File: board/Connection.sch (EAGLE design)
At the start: 42 parts, among them U1 NUCLEO-G431KB, U2 SN65HVD230, U5 ADA4528-1ARMZ-R7

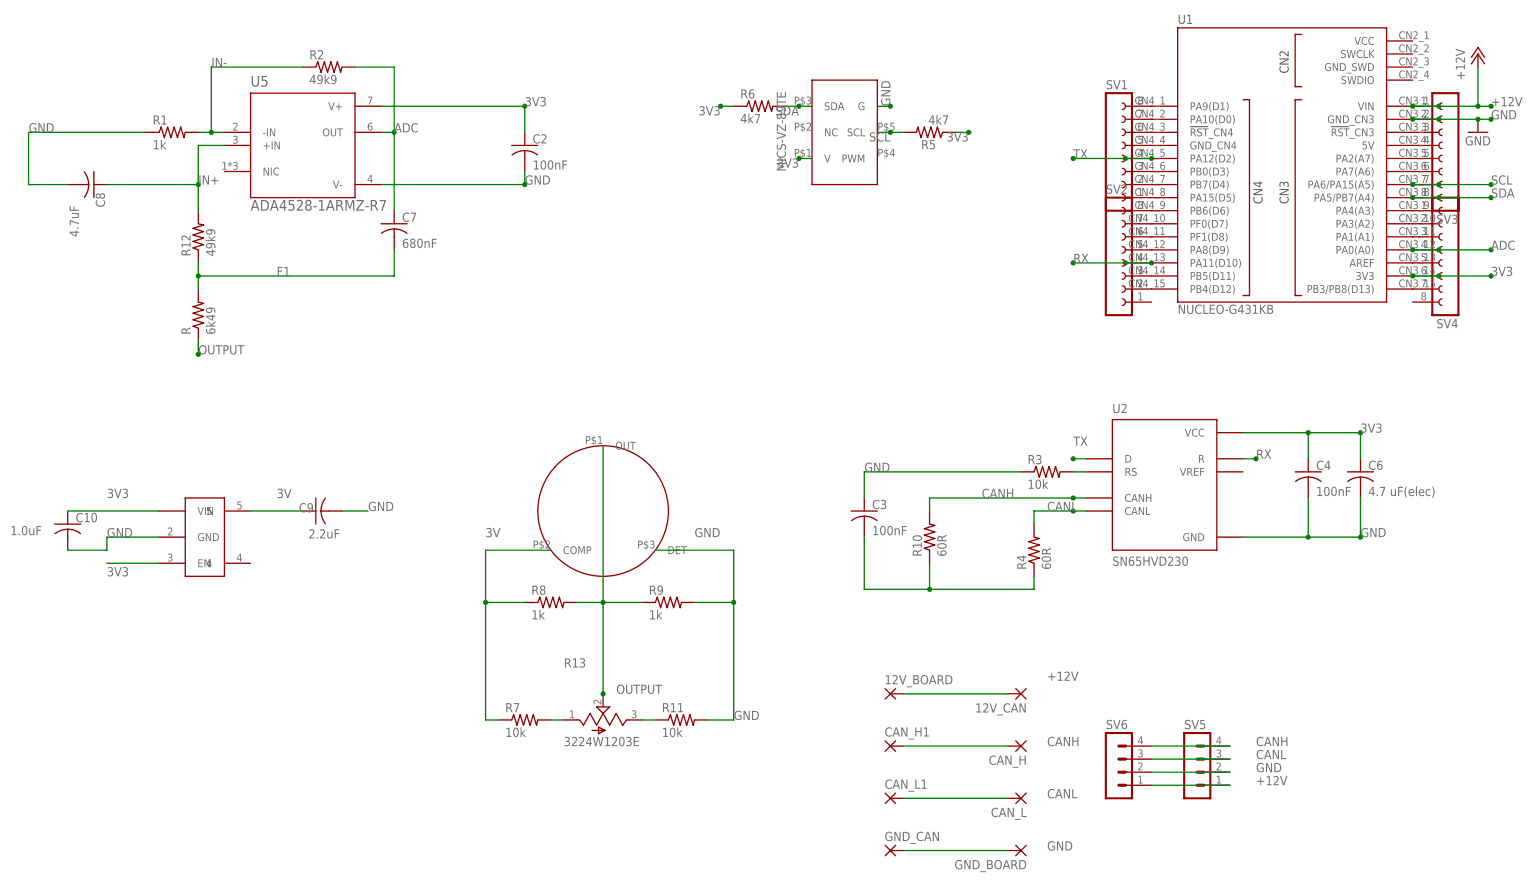
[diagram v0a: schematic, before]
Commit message: move ch4 sensor away from nucleo female header pins for nucleo insertion move the 4pin CAN away from top of the nucleo space the other CAN pins to fit a terminal block
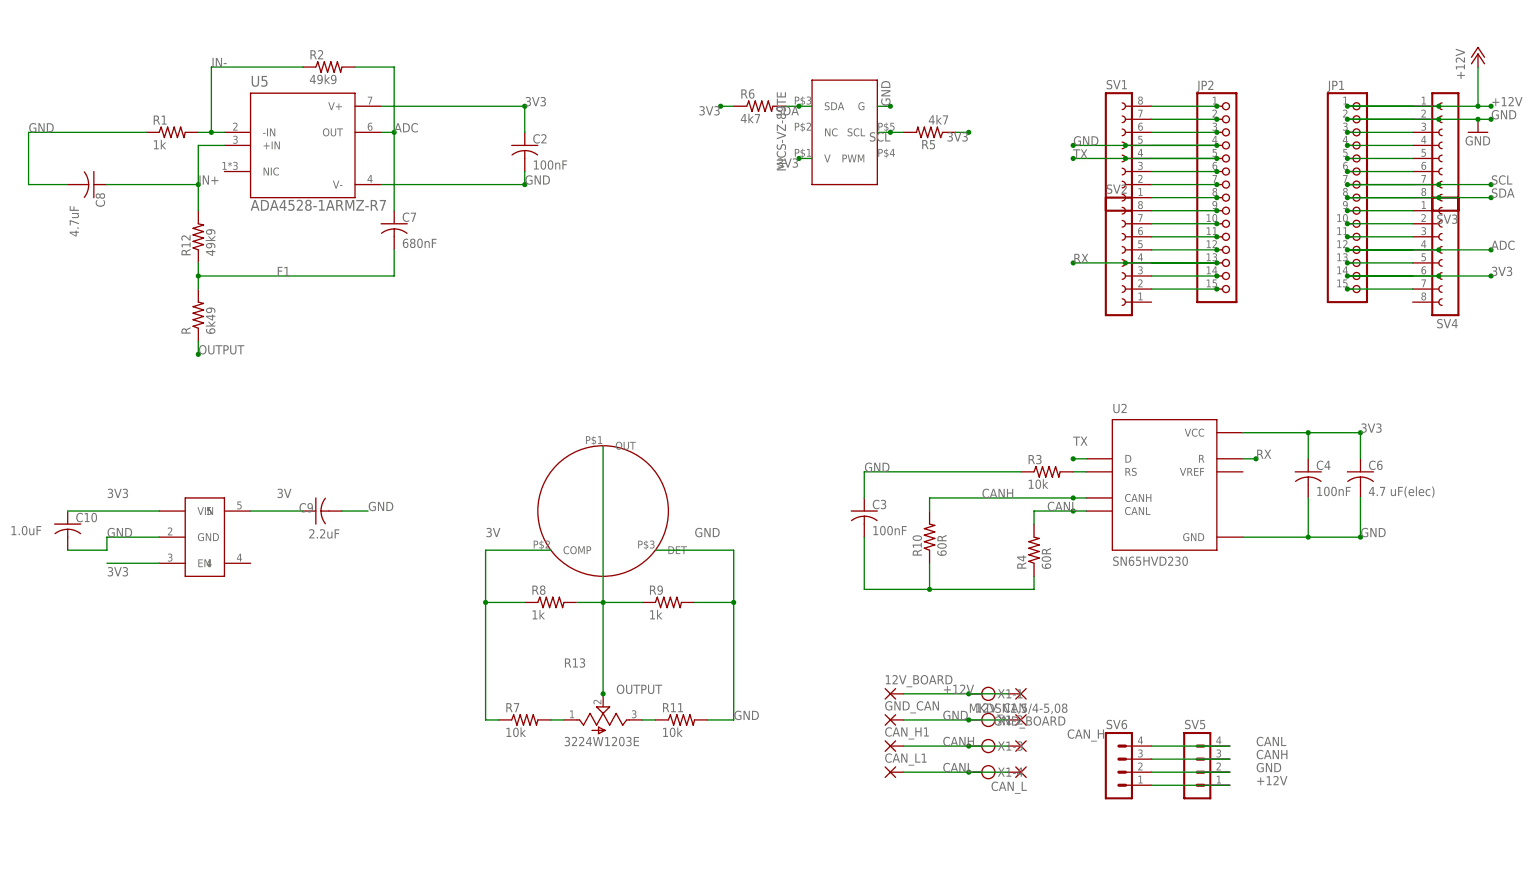
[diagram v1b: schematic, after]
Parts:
- removed U1: NUCLEO-G431KB, NUCLEO-G431KB:NUCLEO-G431KB
- added JP1, JP2: (no value), pinhead:PINHD-1X15
- added X1: MKDSN1,5/4-5,08, con-phoenix-508:MKDSN1,5/4-5,08
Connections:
- removed net N$30: SV1.5, U1.GND_CN4
- net +12V: now also JP1.1, X1-1.KL; no longer U1.VIN
- net 3V3: now also JP1.14; no longer U1.3V3
- net ADC: now also JP1.12; no longer U1.PA0(A0)
- net CANH: now also SV5.3, SV6.3, X1-3.KL; no longer SV5.4, SV6.4
- net CANL: now also SV5.4, SV6.4, X1-4.KL; no longer SV5.3, SV6.3
- net GND: now also JP1.2, JP2.4, SV1.5, X1-2.KL; no longer U1.GND_CN3
- net N$18: now also JP1.3; no longer U1.!RST!_CN3
- net N$19: now also JP1.4; no longer U1.5V
- net N$20: now also JP1.5; no longer U1.PA2(A7)
- net N$22: now also JP1.9; no longer U1.PA4(A3)
- net N$23: now also JP1.10; no longer U1.PA3(A2)
- net N$24: now also JP1.11; no longer U1.PA1(A1)
- net N$25: now also JP1.13; no longer U1.AREF
- net N$26: now also JP1.15; no longer U1.PB3/PB8(D13)
- net N$27: now also JP2.8; no longer U1.PA15(D5)
- net N$28: now also JP2.7; no longer U1.PB7(D4)
- net N$29: now also JP2.6; no longer U1.PB0(D3)
- net N$31: now also JP2.3; no longer U1.!RST!_CN4
- net N$32: now also JP2.2; no longer U1.PA10(D0)
- net N$33: now also JP2.1; no longer U1.PA9(D1)
- net N$34: now also JP2.15; no longer U1.PB4(D12)
- net N$35: now also JP2.14; no longer U1.PB5(D11)
- net N$36: now also JP2.12; no longer U1.PA8(D9)
- net N$37: now also JP2.11; no longer U1.PF1(D8)
- net N$38: now also JP2.10; no longer U1.PF0(D7)
- net N$39: now also JP2.9; no longer U1.PB6(D6)
- net N$6: now also JP1.6; no longer U1.PA7(A6)
- net RX: now also JP2.13; no longer U1.PA11(D10)
- net SCL: now also JP1.7; no longer U1.PA6/PA15(A5)
- net SDA: now also JP1.8; no longer U1.PA5/PB7(A4)
- net TX: now also JP2.5; no longer U1.PA12(D2)
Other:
- moved on the sheet: CAN_L, CAN_L1, GND_BOARD, GND_CAN
